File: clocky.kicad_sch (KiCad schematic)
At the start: 79 parts, among them J1 Bot 50 pin, J2 Bot 40 pin, J3 Top 50 pin, J4 Top 40 pin, J5 Power, J6 JST_PH, J8 Program, Q1 SI2301A, U1 HEF4094B, U10 TMP117xxDRV, U2 HEF4094B, U3 HEF4094B, U4 HEF4094B, U5 HEF4094B, U6 HEF4094B, U7 TPS63060, U8 TPS7A0233PDBV, U9 STM32U031C8Ux, Y1 32768Hz

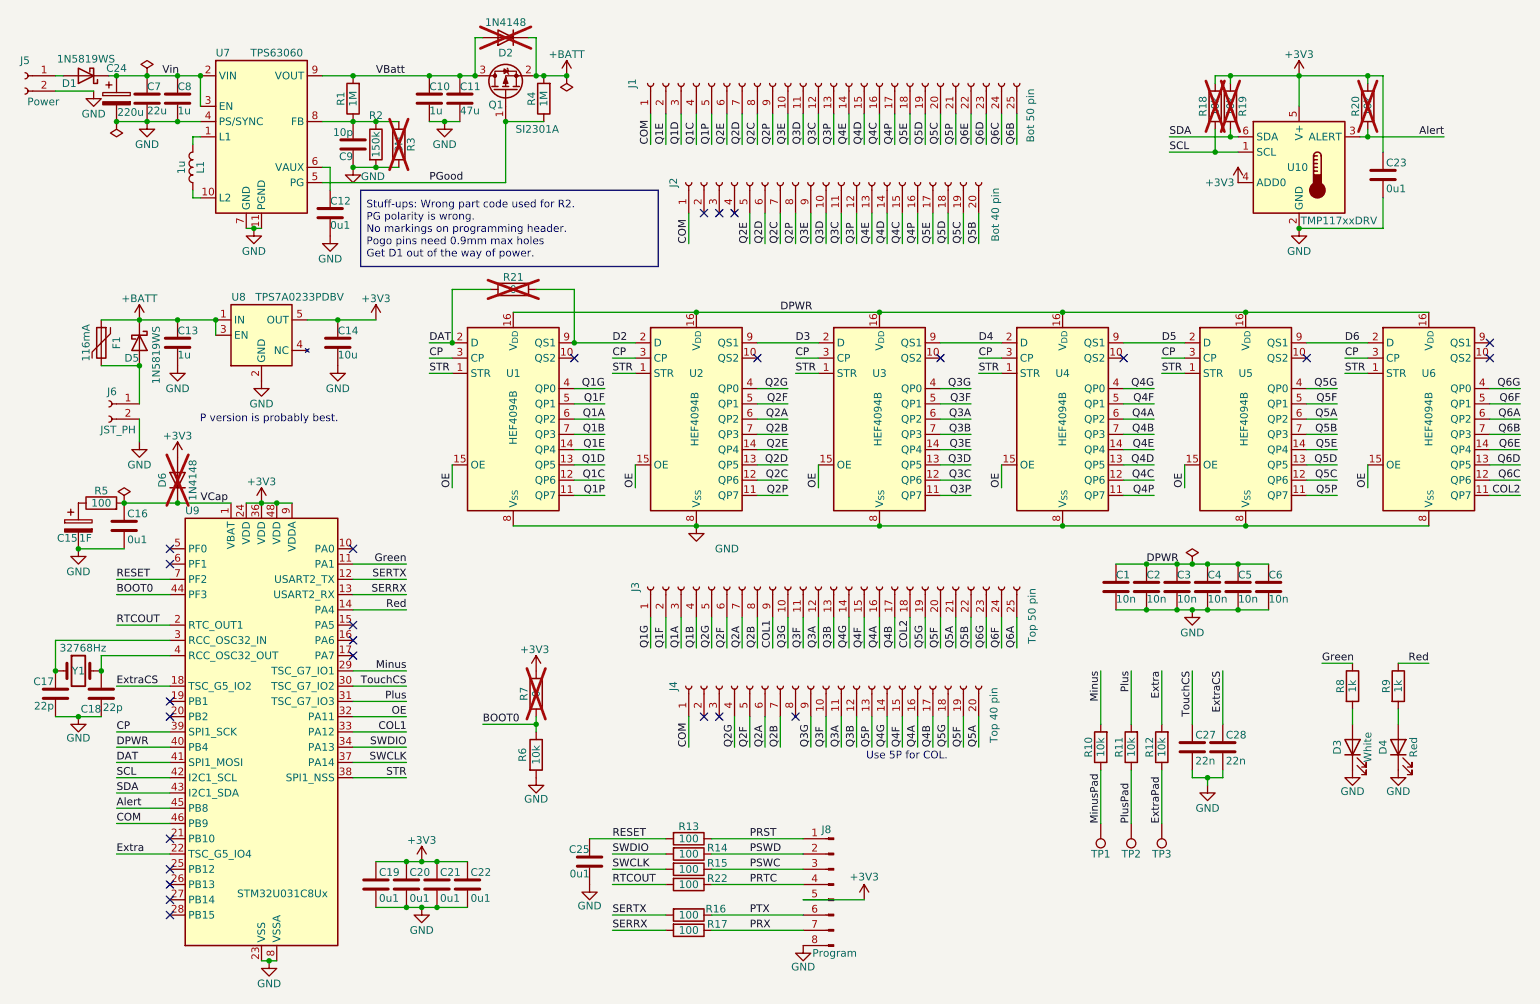
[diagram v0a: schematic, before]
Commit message: Big update to the monitor.
Accell, low side current sense.
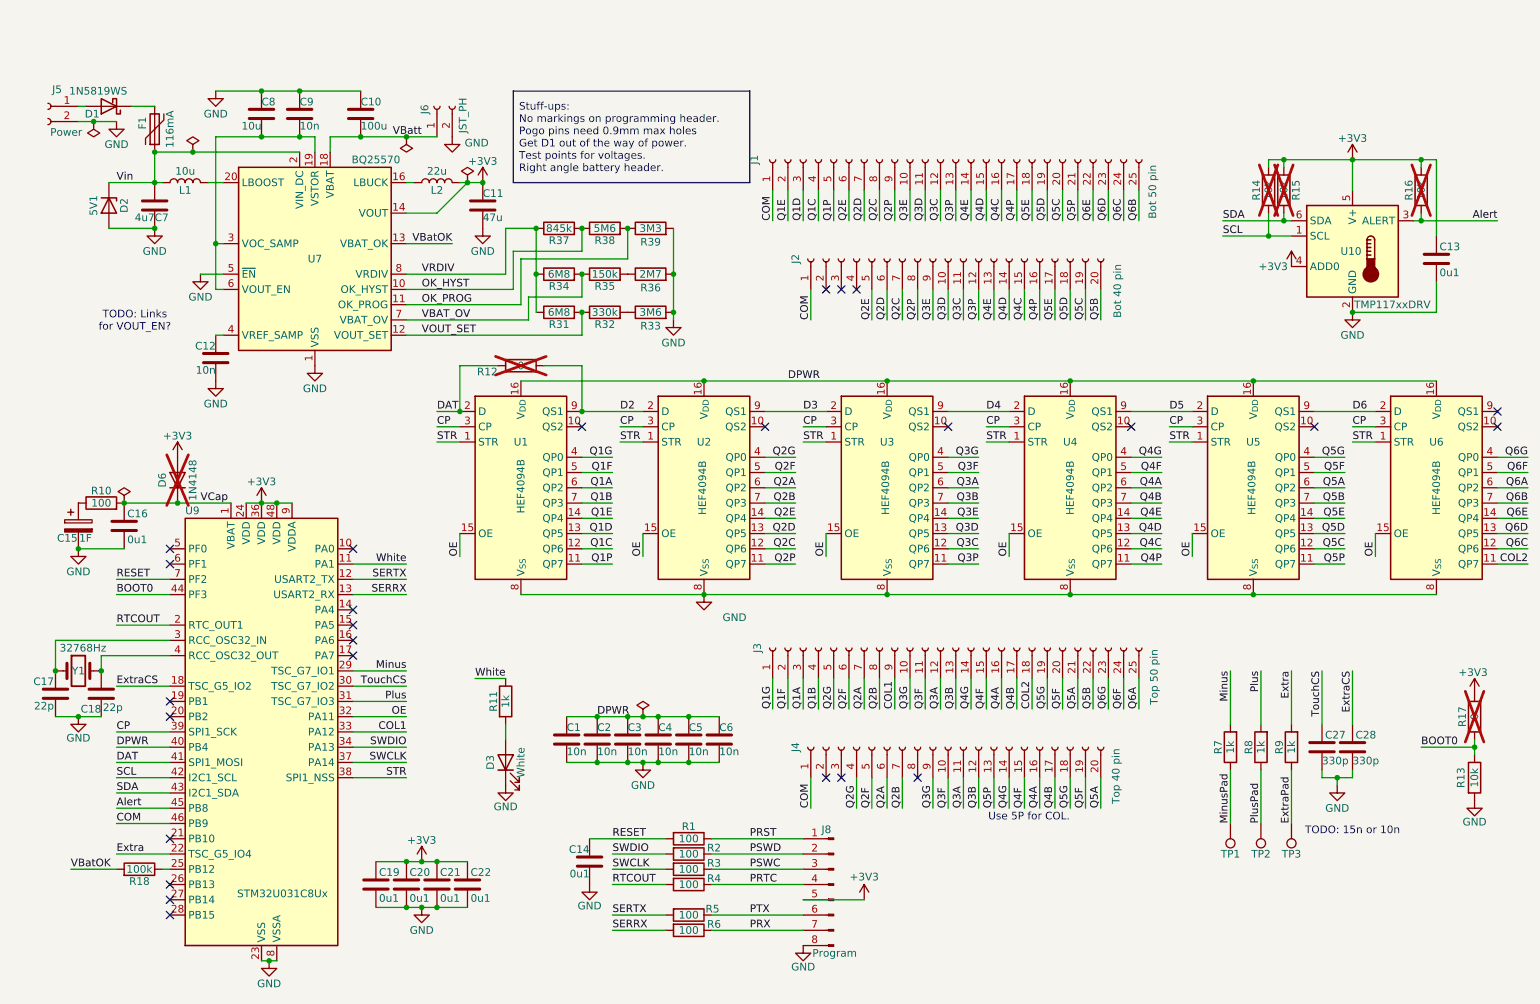
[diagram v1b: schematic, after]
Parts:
- removed C12: 0u1, Capacitor_SMD:C_0402_1005Metric, symbol Device:C
- removed C13: 1u, Capacitor_SMD:C_0402_1005Metric, symbol Device:C
- removed C24: 220u, Capacitor_SMD:CP_Elec_6.3x7.7, symbol Device:C_Polarized
- removed C7: 22u, Capacitor_SMD:C_0805_2012Metric, symbol Device:C
- removed D2: 1N4148, Diode_SMD:D_0603_1608Metric, symbol Device:D
- removed D4: Red, LED_SMD:LED_0603_1608Metric, symbol Device:LED
- removed D5: 1N5819WS, Diode_SMD:D_SOD-323, symbol Diode:1N5819WS
- removed Q1: SI2301A, Package_TO_SOT_SMD:SOT-23, symbol Transistor_FET:AO3401A
- removed R1, R4: 1M, Resistor_SMD:R_0402_1005Metric, symbol Device:R
- removed R3: 3M, Resistor_SMD:R_0603_1608Metric, symbol Device:R
- removed R9: 1k, Resistor_SMD:R_0402_1005Metric, symbol Device:R
- removed U7: TPS63060, Package_SON:Texas_S-PWSON-N10, symbol Regulator_Switching:TPS63060
- removed U8: TPS7A0233PDBV, Package_TO_SOT_SMD:SOT-23-5, symbol Parts:TPS7A0233DBV
- added C10: 100u, Capacitor_SMD:C_1206_3216Metric, symbol Device:C
- added D2: 5V1, Diode_SMD:D_SOD-323, symbol Device:D_Zener
- added L2: 22u, Inductor_SMD:L_0805_2012Metric_Pad1.05x1.20mm_HandSolder, symbol Device:L
- added R18: 100k, Resistor_SMD:R_0402_1005Metric, symbol Device:R
- added R32: 330k, Resistor_SMD:R_0603_1608Metric, symbol Device:R
- added R33: 3M6, Resistor_SMD:R_0603_1608Metric, symbol Device:R
- added R34: 6M8, Resistor_SMD:R_0603_1608Metric, symbol Device:R
- added R35: 150k, Resistor_SMD:R_0603_1608Metric, symbol Device:R
- added R36: 2M7, Resistor_SMD:R_0603_1608Metric, symbol Device:R
- added R37: 845k, Resistor_SMD:R_0603_1608Metric, symbol Device:R
- added R38: 5M6, Resistor_SMD:R_0603_1608Metric, symbol Device:R
- added R39: 3M3, Resistor_SMD:R_0603_1608Metric, symbol Device:R
- added U7: BQ25570, Package_DFN_QFN:QFN-20-1EP_3.5x3.5mm_P0.5mm_EP2x2mm, symbol Battery_Management:BQ25570
- C12: renamed from C14; value 10u -> 10n; JLCPCB C15525 -> C15195
- C27, C28: value 22n -> 330p; footprint Capacitor_SMD:C_0402_1005Metric -> Capacitor_SMD:C_0603_1608Metric; JLCPCB C1532 -> C1664
- C7: renamed from C10; value 1u -> 4u7; footprint Capacitor_SMD:C_0402_1005Metric -> Capacitor_SMD:C_0603_1608Metric; JLCPCB C52923 -> C19666
- C8: value 1u -> 10u; footprint Capacitor_SMD:C_0402_1005Metric -> Capacitor_SMD:C_0603_1608Metric; JLCPCB C52923 -> C15850
- C9: value 10p -> 10n; footprint Capacitor_SMD:C_0603_1608Metric -> Capacitor_SMD:C_0402_1005Metric; JLCPCB (none) -> C15195; now in the parts list
- L1: value 1u -> 10u; footprint Inductor_SMD:L_0805_2012Metric -> Inductor_SMD:L_0805_2012Metric_Pad1.05x1.20mm_HandSolder
- R31: renamed from R2; value 150k -> 6M8; footprint Resistor_SMD:R_0402_1005Metric -> Resistor_SMD:R_0603_1608Metric; JLCPCB C25775 -> (none); now left out of the parts list
- R7: renamed from R10; value 10k -> 1k; JLCPCB C25744 -> C11702
- R8: renamed from R11; value 10k -> 1k; JLCPCB C25744 -> C11702
- R9: renamed from R12; value 10k -> 1k; JLCPCB C25744 -> C11702
- renumbered C23 to C13, C25 to C14, R13 to R1, R5 to R10, R8 to R11, R21 to R12, R6 to R13, R18 to R14, R19 to R15, R20 to R16, R7 to R17, R14 to R2, R15 to R3, R22 to R4, R16 to R5, R17 to R6
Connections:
- net +BATT is gone; now on net Vin: F1.1
- net +3V3: now also C11.1, L2.2, U7.14 (VOUT); no longer C12.1
- net GND: now also C8.1, C10.1, D2.2 (A), R33.2, R36.2, R39.2, U7.1 (VSS), U7.15 (VSS), U7.17 (VSS), U7.21 (VSS), U7.5 (~{EN}), U7.9 (VSS); no longer C8.2, R31.2
- net VBatt: now also J6.1 (Pin_1), C10.2, U7.18 (VBAT); no longer C11.1, C7.1
- net Vin: now also C7.1, L1.1, D2.1 (K), U7.2 (VIN_DC); no longer C8.1, D1.1 (K)
- net at U9.25 (PB12): now also R18.1
- net at F1.2: now also D1.1 (K); no longer J6.1 (Pin_1)
- net at C9.2: now also C8.2, U7.19 (VSTOR), U7.3 (VOC_SAMP), U7.6 (VOUT_EN); no longer R31.1
- net at L1.2: now also U7.20 (LBOOST)
- net Green renamed White
- net Red: no longer names the net of U9.14 (PA4)
- new net: L2.1, U7.16 (LBUCK)
- new net: C12.1, U7.4 (VREF_SAMP)
- new net: R35.2, R36.1
- new net: R32.2, R33.1
- new net OK_HYST: R37.2, R38.1, U7.10 (OK_HYST)
- new net OK_PROG: R38.2, R39.1, U7.11 (OK_PROG)
- new net VBAT_OV: R34.2, R35.1, U7.7 (VBAT_OV)
- new net VBatOK: R18.2, U7.13 (VBAT_OK)
- new net VOUT_SET: R31.2, R32.1, U7.12 (VOUT_SET)
- new net VRDIV: R31.1, R34.1, R37.1, U7.8 (VRDIV)
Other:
- note added: "TODO: 15n or 10n"
- note added: "TODO: Links for VOUT_EN?"
- note removed: "P version is probably best."
- moved on the sheet: C1, C11, C12, C13, C2, C27, C28, C3, C4, C5, C6, C7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

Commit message: Tweaks.  Fabbing.
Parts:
- removed F1: 116mA, Resistor_SMD:R_0805_2012Metric_Pad1.20x1.40mm_HandSolder, symbol Device:Polyfuse
- added C23: 1u, Capacitor_SMD:C_0402_1005Metric, symbol Device:C
- added R19: 0R, Resistor_SMD:R_0603_1608Metric, symbol Device:R
- added TP4, TP5, TP6, TP7: TestPoint_Probe, Parts:TestPoint, symbol Connector:TestPoint_Probe
- C11: footprint Capacitor_SMD:C_1206_3216Metric -> Capacitor_SMD:C_0805_2012Metric; JLCPCB C96123 -> C16780
- C27, C28: footprint Capacitor_SMD:C_0603_1608Metric -> Capacitor_SMD:C_0402_1005Metric; JLCPCB C1664 -> C13533
- C7: value 4u7 -> 10u; JLCPCB C19666 -> C19702
- R18: value 100k -> 0R; footprint Resistor_SMD:R_0402_1005Metric -> Resistor_SMD:R_0603_1608Metric; JLCPCB (none) -> C21189
- R25: renamed from R35; JLCPCB (none) -> C22807; now in the parts list
- R28: renamed from R32; JLCPCB (none) -> C23137; now in the parts list
- renumbered R37 to R21, R38 to R22, R39 to R23, R34 to R24, R36 to R26, R31 to R27, R33 to R29
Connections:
- net +3V3: now also C23.1, TP6.1
- net GND: now also J6.1 (Pin_1), C23.2, TP4.1; no longer J6.2 (Pin_2)
- net VBatOK: now also U9.25 (PB12), R19.1; no longer R18.2
- net VBatt: now also J6.2 (Pin_2), TP5.1; no longer J6.1 (Pin_1)
- net Vin: now also D1.1 (K), TP7.1
- net VStor: now reaches R18.1
- net VStor: now also C8.2, C9.2, U7.19 (VSTOR), U7.3 (VOC_SAMP); no longer U9.25 (PB12)
- new net: R18.2, R19.2, U7.6 (VOUT_EN)
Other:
- note removed: "TODO: Links for VOUT_EN?"
- moved on the sheet: C11, D1, J5, J6, R21, R22, R23, R24, R25, R26, R27, R28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

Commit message: Update notes on schematic.
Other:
- note added: "Alert got hot wired to PC13 with R4 removed."
- note removed: "TODO: 15n or 10n"
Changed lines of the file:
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@@
 	(generator_version "9.0")
 	(paper "A4")
-	(text "TODO: 15n or 10n"
+	(text "Use 5P for COL."
 		(exclude_from_sim no)
-		(at 246.38 156.21 0)
+		(at 192.532 153.924 0)
 		(effects
 			(font
@@
 		)
 	)
-	(text "Use 5P for COL."
+	(text "Alert got hot wired to PC13\nwith R4 removed."
 		(exclude_from_sim no)
-		(at 192.532 153.924 0)
+		(at 216.408 72.39 0)
 		(effects
 			(font
 				(size 1.27 1.27)
 			)
+			(justify left)
 		)
 	)
@@
 		)
 		(property "Value" "GND"
-			(at 143.51 120.65 0)
+			(at 138.43 120.65 0)
 			(effects
 				(font

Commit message: Update resistor values.
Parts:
- R21: value 845k -> 634k
- R22: value 5M6 -> 6M8
- R23: value 3M3 -> 3M6
- R25: value 150k -> 274k
- R26: value 2M7 -> 3M6
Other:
- note added: "3.15V,3.49V"
- note added: "3.3V"
- note added: "5V"
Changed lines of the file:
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@@
 	(generator_version "9.0")
 	(paper "A4")
+	(text "5V"
+		(exclude_from_sim no)
+		(at 139.446 63.5 0)
+		(effects
+			(font
+				(size 1.27 1.27)
+			)
+		)
+	)
+	(text "3.3V\n"
+		(exclude_from_sim no)
+		(at 140.462 69.85 0)
+		(effects
+			(font
+				(size 1.27 1.27)
+			)
+		)
+	)
+	(text "3.15V,3.49V"
+		(exclude_from_sim no)
+		(at 143.256 56.388 0)
+		(effects
+			(font
+				(size 1.27 1.27)
+			)
+		)
+	)
 	(text "Use 5P for COL."
 		(exclude_from_sim no)
@@
 			)
 		)
-		(property "Value" "845k"
+		(property "Value" "634k"
 			(at 118.11 55.88 90)
 			(effects
@@
 			)
 		)
-		(property "Value" "3M3"
+		(property "Value" "3M6"
 			(at 133.35 55.88 90)
 			(effects
@@
 			)
 		)
-		(property "Value" "2M7"
+		(property "Value" "3M6"
 			(at 133.35 63.5 90)
 			(effects
@@
 			)
 		)
-		(property "Value" "5M6"
+		(property "Value" "6M8"
 			(at 125.73 55.88 90)
 			(effects
@@
 			)
 		)
-		(property "Value" "150k"
+		(property "Value" "274k"
 			(at 125.73 63.5 90)
 			(effects

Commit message: Add clock drive and crash address.
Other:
- note added: "J6 got labels swapped on board. Connectors are crap for right-angle. VBatOk is not that great. Alert is not on a wake-up, rewire to pin 2, replace RTC out. Bring batt & super-cap to front. Current limit somewhere?"
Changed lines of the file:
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@@
 	(generator_version "9.0")
 	(paper "A4")
+	(text "J6 got labels swapped on board.\nConnectors are crap for right-angle.\nVBatOk is not that great.\nAlert is not on a wake-up,\nrewire to pin 2, replace RTC out.\nBring batt & super-cap to front.\nCurrent limit somewhere?"
+		(exclude_from_sim no)
+		(at 113.284 45.466 0)
+		(effects
+			(font
+				(size 1.27 1.27)
+			)
+			(justify left)
+		)
+	)
 	(text "5V"
 		(exclude_from_sim no)

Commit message: Update resistor values.
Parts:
- R22: value 6M8 -> 6M2
- R23, R26: value 3M6 -> 3M9
- R24: value 6M8 -> 5M1
- R25: value 274k -> 330k
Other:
- note added: "2.86V, 3.13V"
- note added: "4V"
- note removed: "3.15V,3.49V"
- note removed: "5V"
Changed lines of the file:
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@@
 		)
 	)
-	(text "5V"
+	(text "4V"
 		(exclude_from_sim no)
 		(at 139.446 63.5 0)
@@
 		)
 	)
-	(text "3.15V,3.49V"
+	(text "2.86V, 3.13V"
 		(exclude_from_sim no)
 		(at 143.256 56.388 0)
@@
 			)
 		)
-		(property "Value" "3M6"
+		(property "Value" "3M9"
 			(at 133.35 55.88 90)
 			(effects
@@
 			)
 		)
-		(property "Value" "3M6"
+		(property "Value" "3M9"
 			(at 133.35 63.5 90)
 			(effects
@@
 			)
 		)
-		(property "Value" "6M8"
+		(property "Value" "6M2"
 			(at 125.73 55.88 90)
 			(effects
@@
 			)
 		)
-		(property "Value" "274k"
+		(property "Value" "330k"
 			(at 125.73 63.5 90)
 			(effects
@@
 			)
 		)
-		(property "Value" "6M8"
+		(property "Value" "5M1"
 			(at 118.11 63.5 90)
 			(effects

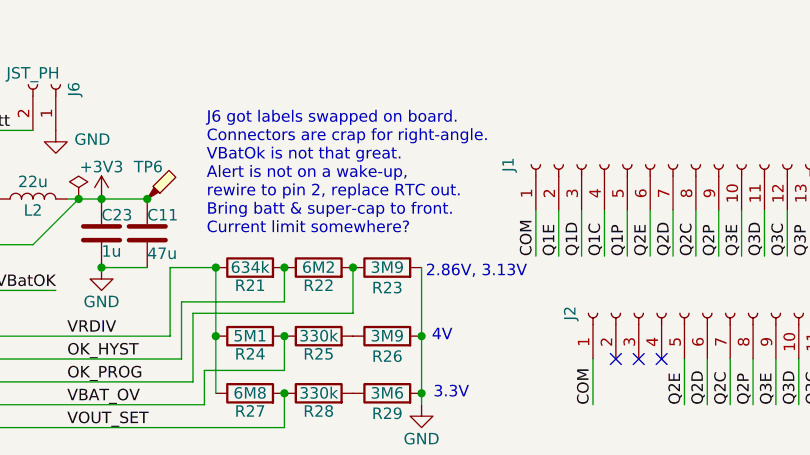
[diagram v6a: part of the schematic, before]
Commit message: Simplify and fix and temperature handling.
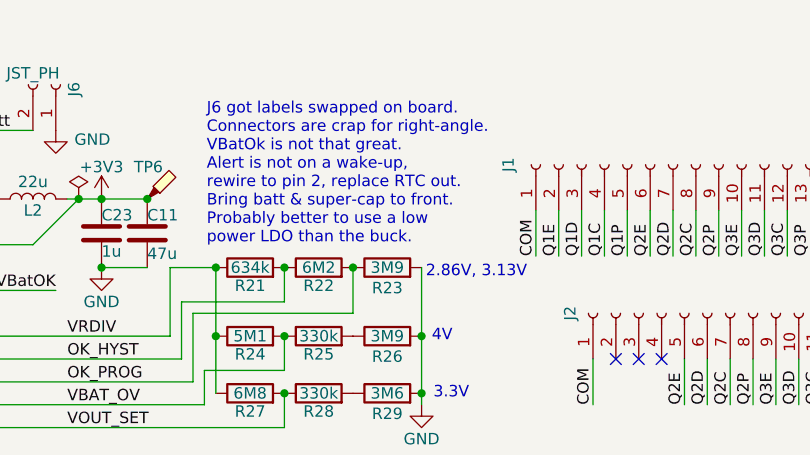
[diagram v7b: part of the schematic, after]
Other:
- note added: "J6 got labels swapped on board. Connectors are crap for right-angle. VBatOk is not that great. Alert is not on a wake-up, rewire to pin 2, replace RTC out. Bring batt & super-cap to front. Probably better to use a low power LDO than the buck."
- note removed: "J6 got labels swapped on board. Connectors are crap for right-angle. VBatOk is not that great. Alert is not on a wake-up, rewire to pin 2, replace RTC out. Bring batt & super-cap to front. Current limit somewhere?"
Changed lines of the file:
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@@
 	(generator_version "9.0")
 	(paper "A4")
-	(text "J6 got labels swapped on board.\nConnectors are crap for right-angle.\nVBatOk is not that great.\nAlert is not on a wake-up,\nrewire to pin 2, replace RTC out.\nBring batt & super-cap to front.\nCurrent limit somewhere?"
+	(text "J6 got labels swapped on board.\nConnectors are crap for right-angle.\nVBatOk is not that great.\nAlert is not on a wake-up,\nrewire to pin 2, replace RTC out.\nBring batt & super-cap to front.\nProbably better to use a low\npower LDO than the buck."
 		(exclude_from_sim no)
 		(at 113.284 45.466 0)
